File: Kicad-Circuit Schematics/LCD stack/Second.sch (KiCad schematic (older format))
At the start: 4 parts, among them P1 CONN_20X2, P2 CONN_17, U1 MCP23017

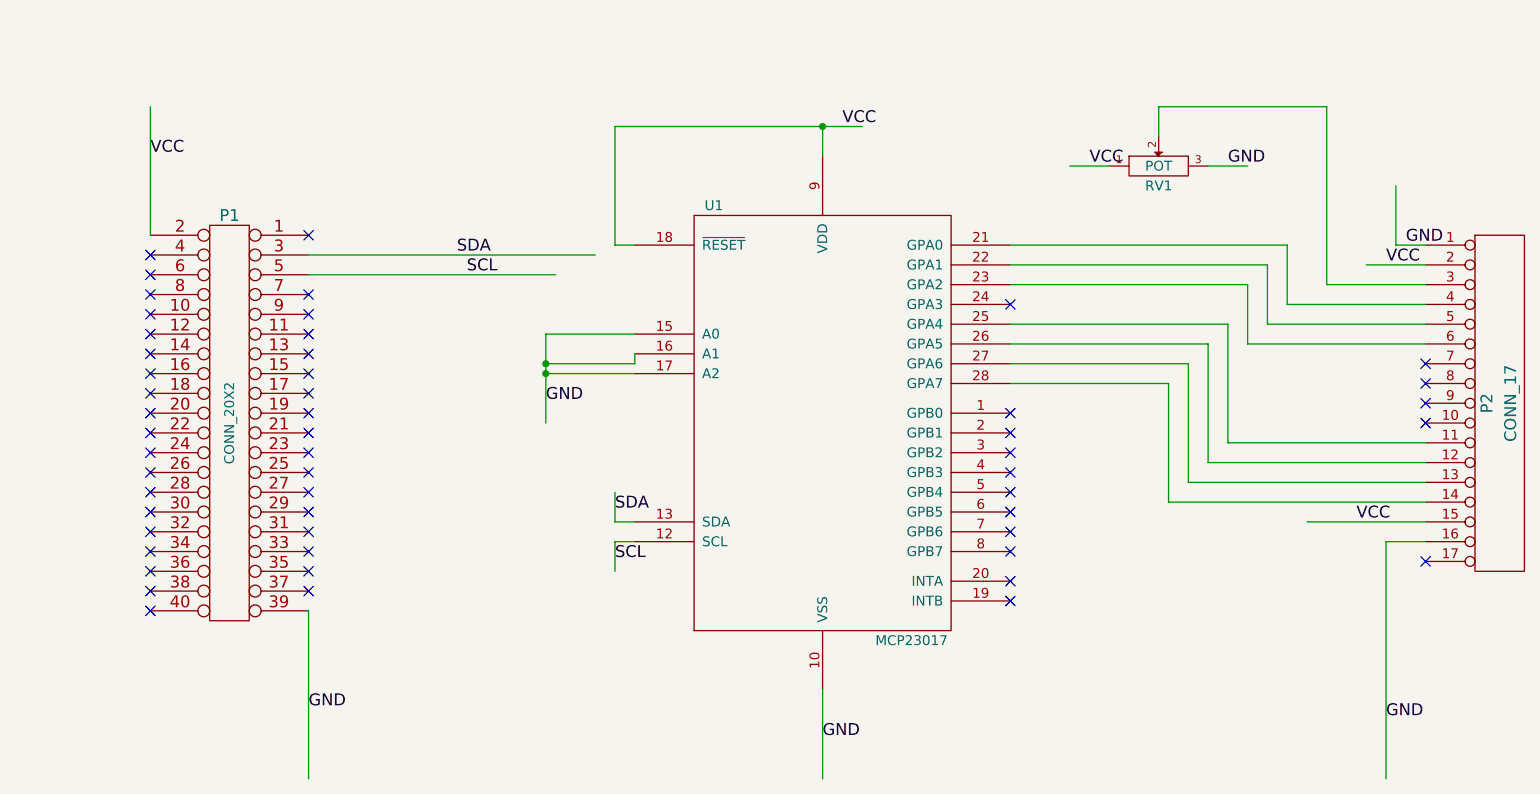
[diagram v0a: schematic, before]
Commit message: Final designs added
Contains the pcb layout and schematics of 3 stacks
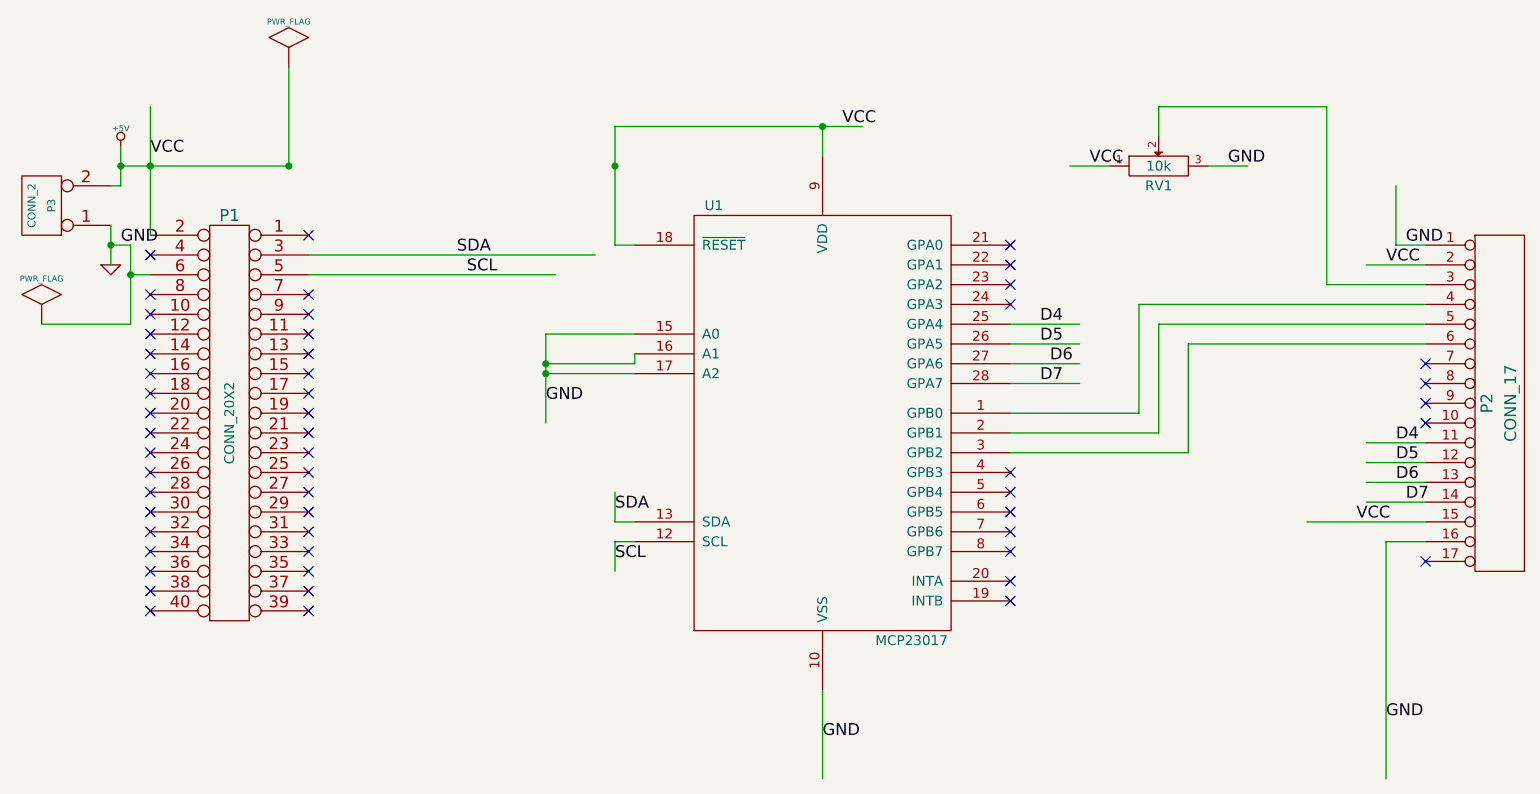
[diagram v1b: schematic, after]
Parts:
- added P3: CONN_2, symbol CONN_2
- RV1: value POT -> 10k
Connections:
- net labels added: +5V, D4, D5, D6, D7
- wire segments 51 -> 55
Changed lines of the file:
@@
-EESchema Schematic File Version 2  date 26/06/2015 16:22:58
+EESchema Schematic File Version 2  date 07/07/2015 20:15:06
 LIBS:power
 LIBS:device
@@
 Sheet 1 1
 Title "LCD interface"
-Date "26 jun 2015"
+Date "7 jul 2015"
 Rev ""
 Comp ""
@@
 Comment4 ""
 $EndDescr
+Text Label 7900 4200 0    60   ~ 0
+D7
+Text Label 7850 4100 0    60   ~ 0
+D6
+Text Label 7850 4000 0    60   ~ 0
+D5
+Text Label 7850 3900 0    60   ~ 0
+D4
+Text Label 6050 3600 0    60   ~ 0
+D7
+Text Label 6100 3500 0    60   ~ 0
+D6
+Text Label 6050 3400 0    60   ~ 0
+D5
+Text Label 6050 3300 0    60   ~ 0
+D4
+NoConn ~ 5900 4450
+NoConn ~ 5900 4350
+NoConn ~ 5900 4250
+NoConn ~ 5900 4150
+NoConn ~ 5900 4050
+NoConn ~ 5900 2900
+NoConn ~ 5900 3000
+NoConn ~ 5900 3100
+Wire Wire Line
+	5900 3300 6250 3300
+Wire Wire Line
+	5900 3500 6250 3500
+Wire Wire Line
+	8000 4100 7700 4100
+Wire Wire Line
+	8000 3900 7700 3900
+Wire Wire Line
+	8000 3300 6650 3300
+Wire Wire Line
+	5900 3750 6550 3750
+Wire Wire Line
+	6550 3750 6550 3200
+Wire Wire Line
+	6550 3200 8000 3200
+Wire Wire Line
+	1400 2500 2250 2500
+Connection ~ 2250 2500
+Connection ~ 1450 3050
+Wire Wire Line
+	1450 3300 1450 2900
+Wire Wire Line
+	1450 3300 1000 3300
+Connection ~ 1350 2900
+Wire Wire Line
+	1450 2900 1350 2900
+Wire Wire Line
+	1450 3050 1550 3050
+Wire Wire Line
+	1350 2800 1350 3000
+Wire Wire Line
+	1400 2400 1400 2600
+Wire Wire Line
+	1400 2600 1350 2600
+Connection ~ 3550 3500
+Wire Wire Line
+	3550 3500 4000 3500
+Wire Wire Line
+	4000 3500 4000 3450
+Wire Wire Line
+	6900 2500 7100 2500
+Connection ~ 4950 2300
+Wire Wire Line
+	5150 2300 3900 2300
+Wire Wire Line
+	3900 4550 3900 4400
+Wire Wire Line
+	3900 4400 4000 4400
+Wire Wire Line
+	1550 2200 1550 2850
+Wire Wire Line
+	3800 2950 2350 2950
+Wire Wire Line
+	6650 2350 6650 2200
+Wire Wire Line
+	6650 2200 7500 2200
+Wire Wire Line
+	7500 2200 7500 3100
+Wire Wire Line
+	7500 3100 8000 3100
+Wire Wire Line
+	7800 5600 7800 4400
+Wire Wire Line
+	7800 4400 8000 4400
+Wire Wire Line
+	4950 5600 4950 5150
+Wire Wire Line
+	7850 2600 7850 2900
+Wire Wire Line
+	7850 2900 8000 2900
+Wire Wire Line
+	7700 3000 8000 3000
+Wire Wire Line
+	8000 4300 7400 4300
+Wire Wire Line
+	2350 3050 3600 3050
+Wire Wire Line
+	4000 4300 3900 4300
+Wire Wire Line
+	3900 4300 3900 4150
+Wire Wire Line
+	4000 2900 3900 2900
+Wire Wire Line
+	3900 2900 3900 2300
+Wire Wire Line
+	4950 2300 4950 2450
+Wire Wire Line
+	6400 2500 6200 2500
+Wire Wire Line
+	4000 3350 3550 3350
+Wire Wire Line
+	3550 3350 3550 3800
+Wire Wire Line
+	4000 3550 3550 3550
+Connection ~ 3550 3550
+Connection ~ 1400 2500
+Connection ~ 1550 2500
+Connection ~ 3900 2500
+Wire Wire Line
+	2250 2500 2250 2000
+Wire Wire Line
+	6650 3300 6650 3850
+Wire Wire Line
+	6650 3850 5900 3850
+Wire Wire Line
+	8000 3400 6800 3400
+Wire Wire Line
+	6800 3400 6800 3950
+Wire Wire Line
+	6800 3950 5900 3950
+Wire Wire Line
+	8000 4000 7700 4000
+Wire Wire Line
+	8000 4200 7700 4200
+Wire Wire Line
+	5900 3600 6250 3600
+Wire Wire Line
+	5900 3400 6250 3400
+$Comp
+L PWR_FLAG #FLG01
+U 1 1 559106F5
+P 2250 2000
+F 0 "#FLG01" H 2250 2270 30  0001 C CNN
+F 1 "PWR_FLAG" H 2250 2230 30  0000 C CNN
+	1    2250 2000
+	1    0    0    -1
+$EndComp
+$Comp
+L PWR_FLAG #FLG02
+U 1 1 55910180
+P 1000 3300
+F 0 "#FLG02" H 1000 3570 30  0001 C CNN
+F 1 "PWR_FLAG" H 1000 3530 30  0000 C CNN
+	1    1000 3300
+	1    0    0    -1
+$EndComp
+NoConn ~ 2350 4750
+Text Label 1400 2900 0    60   ~ 0
+GND
+$Comp
+L GND #PWR03
+U 1 1 559100DC
+P 1350 3000
+F 0 "#PWR03" H 1350 3000 30  0001 C CNN
+F 1 "GND" H 1350 2930 30  0001 C CNN
+	1    1350 3000
+	1    0    0    -1
+$EndComp
+$Comp
+L +5V #PWR04
+U 1 1 559100C7
+P 1400 2400
+F 0 "#PWR04" H 1400 2490 20  0001 C CNN
+F 1 "+5V" H 1400 2490 30  0000 C CNN
+	1    1400 2400
+	1    0    0    -1
+$EndComp
+$Comp
+L CONN_2 P3
+U 1 1 559100AB
+P 1000 2700
+F 0 "P3" V 950 2700 40  0000 C CNN
+F 1 "CONN_2" V 1050 2700 40  0000 C CNN
+	1    1000 2700
+	-1   0    0    1
+$EndComp
 Text Label 3550 3700 0    60   ~ 0
 GND
-Connection ~ 3550 3550
-Wire Wire Line
-	4000 3550 3550 3550
-Wire Wire Line
-	3550 3800 3550 3350
-Wire Wire Line
-	3550 3350 4000 3350
-Wire Wire Line
-	6400 2500 6200 2500
-Wire Wire Line
-	4950 2300 4950 2450
-Wire Wire Line
-	3900 2900 3900 2300
-Wire Wire Line
-	3900 2900 4000 2900
-Wire Wire Line
-	3900 4150 3900 4300
-Wire Wire Line
-	3900 4300 4000 4300
-Wire Wire Line
-	2350 3050 3600 3050
-Wire Wire Line
-	2350 4750 2350 5600
-Wire Wire Line
-	8000 4300 7400 4300
-Wire Wire Line
-	8000 4100 6800 4100
-Wire Wire Line
-	6800 4100 6800 3500
-Wire Wire Line
-	6800 3500 5900 3500
-Wire Wire Line
-	5900 3300 7000 3300
-Wire Wire Line
-	7000 3300 7000 3900
-Wire Wire Line
-	7000 3900 8000 3900
-Wire Wire Line
-	8000 3400 7100 3400
-Wire Wire Line
-	7100 3400 7100 3100
-Wire Wire Line
-	7100 3100 5900 3100
-Wire Wire Line
-	5900 2900 7300 2900
-Wire Wire Line
-	7300 2900 7300 3200
-Wire Wire Line
-	7300 3200 8000 3200
-Wire Wire Line
-	7700 3000 8000 3000
-Wire Wire Line
-	8000 2900 7850 2900
-Wire Wire Line
-	7850 2900 7850 2600
-Wire Wire Line
-	4950 5600 4950 5150
-Wire Wire Line
-	8000 4400 7800 4400
-Wire Wire Line
-	7800 4400 7800 5600
-Wire Wire Line
-	8000 3100 7500 3100
-Wire Wire Line
-	7500 3100 7500 2200
-Wire Wire Line
-	7500 2200 6650 2200
-Wire Wire Line
-	6650 2200 6650 2350
-Wire Wire Line
-	7200 3000 7200 3300
-Wire Wire Line
-	7200 3000 5900 3000
-Wire Wire Line
-	7200 3300 8000 3300
-Wire Wire Line
-	8000 4000 6900 4000
-Wire Wire Line
-	6900 4000 6900 3400
-Wire Wire Line
-	6900 3400 5900 3400
-Wire Wire Line
-	8000 4200 6700 4200
-Wire Wire Line
-	6700 4200 6700 3600
-Wire Wire Line
-	6700 3600 5900 3600
-Wire Wire Line
-	3800 2950 2350 2950
-Wire Wire Line
-	1550 2200 1550 2850
-Wire Wire Line
-	4000 4400 3900 4400
-Wire Wire Line
-	3900 4400 3900 4550
-Wire Wire Line
-	3900 2300 5150 2300
-Connection ~ 4950 2300
-Wire Wire Line
-	6900 2500 7100 2500
-Wire Wire Line
-	4000 3450 4000 3500
-Wire Wire Line
-	4000 3500 3550 3500
-Connection ~ 3550 3500
 Text Label 7650 4300 0    60   ~ 0
 VCC
@@
 Text Label 3100 2950 0    60   ~ 0
 SDA
-Text Label 2350 5250 0    60   ~ 0
-GND
 Text Label 7900 2900 0    60   ~ 0
 GND
@@
 GND
 NoConn ~ 1550 2950
-NoConn ~ 1550 3050
 NoConn ~ 1550 3150
 NoConn ~ 1550 3250
@@
 NoConn ~ 5900 4700
 NoConn ~ 5900 4600
-NoConn ~ 5900 4450
-NoConn ~ 5900 4350
-NoConn ~ 5900 4250
-NoConn ~ 5900 4150
-NoConn ~ 5900 4050
-NoConn ~ 5900 3950
-NoConn ~ 5900 3850
-NoConn ~ 5900 3750
 NoConn ~ 5900 3200
 $Comp
@@
 P 6650 2500
 F 0 "RV1" H 6650 2400 50  0000 C CNN
-F 1 "POT" H 6650 2500 50  0000 C CNN
+F 1 "10k" H 6650 2500 50  0000 C CNN
 	1    6650 2500
 	1    0    0    -1
